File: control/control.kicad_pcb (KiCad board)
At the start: 2 copper layers, 140 x 103.2 mm, 136 parts, among them IC1 TJA1040, IC2 MAX481, IC3 ST232BD, IC4 ATMEGA128-A, IC5 ST232BD, IC6 FT232RL, J4 POWER, P1 SENSOR, P10 DB9, P11 USB_B, P12 USB_M6, P13 DB9, P2 I2C0, P3 I2C1, P4 I2C2, P5 COIN, P6 BILL, P7 ISP, P8 12V, P9 5V, X1 16MHz

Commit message: Updated control board for KiCad 4.0
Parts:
- added R71: DNP, Resistors_SMD:R_0805_HandSoldering, F.Cu at (111.7, 153.8)
- C1, C10, C11, C12, C13, C14, C15, C16, C17, C18, C19, C2, C20, C21, C22, C23, C25, C27, C28, C29, C3, C30, C31, C4, C5, C6, C7, C8, C9: footprint R0805 -> Capacitors_SMD:C_0805_HandSoldering
- C24, C26, C32: footprint C1V5 -> Capacitors_ThroughHole:C_Radial_D5_L11_P2.5
- D1: value RED -> LED805; footprint LED-0805 -> LEDs:LED-0805
- D2, D3: value GREEN -> LED805; footprint LED-0805 -> LEDs:LED-0805
- D4: value TX -> LED805; footprint LED-0805 -> LEDs:LED-0805
- D5: value RX -> LED805; footprint LED-0805 -> LEDs:LED-0805
- IC1: footprint SO8N -> Housings_SOIC:SOIC-8_3.9x4.9mm_Pitch1.27mm
- IC2: value MAX481 -> DNP MAX481CSA; footprint SO8N -> Housings_SOIC:SOIC-8_3.9x4.9mm_Pitch1.27mm
- IC3, IC5: footprint SO16N -> Housings_SOIC:SOIC-16_3.9x9.9mm_Pitch1.27mm
- IC4: footprint TQFP64 -> Housings_QFP:TQFP-64_14x14mm_Pitch0.8mm
- IC6: footprint SSOP28 -> Housings_SSOP:SSOP-28_5.3x10.2mm_Pitch0.65mm
- J4, P1: footprint he10-16ds -> Pin_Headers:Pin_Header_Straight_2x08
- JP1: value FLASH -> 1-2 FLASH EN; footprint SIL-3 -> Pin_Headers:Pin_Header_Straight_1x03
- JP2: value RESET -> 1-2 RESET; footprint SIL-3 -> Pin_Headers:Pin_Header_Straight_1x03
- L1: footprint wuerth_elektronik_v5-WE-PD2_S -> matemat:wuerth_elektronik_v5-WE-PD2_S
- P10, P13: footprint DB9MCS -> matemat:DB9MCS
- P11: footprint USB_B -> Connect:USB_B
- P12: value USB_M6 -> USB_OTG; footprint USB_MINI_B_6 -> Connect:USB_Micro-B
- P2, P3, P4, P5: footprint he10-10ds -> Pin_Headers:Pin_Header_Straight_2x05
- P6: footprint HE10_26DS -> Pin_Headers:Pin_Header_Straight_2x13
- P7: footprint pin_array_3x2 -> Pin_Headers:Pin_Header_Straight_2x03
- P8, P9: footprint Bornier_B2_Phoenix -> matemat:Bornier_B2_Phoenix
- R1, R10, R11, R12, R13, R14, R15, R16, R17, R18, R19, R2, R20, R21, R22, R23, R24, R25, R26, R27, R28, R29, R3, R30, R31, R32, R33, R34, R35, R36, R37, R38, R39, R4, R40, R41, R42, R43, R44, R45, R46, R47, R48, R49, R5, R50, R51, R52, R53, R54, R55, R56, R57, R58, R59, R6, R60, R61, R62, R63, R64, R65, R66, R67, R68, R69, R7, R70, R8, R9: footprint R0805 -> Resistors_SMD:R_0805_HandSoldering
- TP1, TP2, TP3, TP4: footprint TROU3 -> Mounting_Holes:MountingHole_3mm
- X1: footprint Q_49U3HMS -> Crystals:Q_49U3HMS
- moved P6 15.4 mm to (102.1, 62.9), turned to 90 degrees
- moved J4 9.01 mm to (141.1, 126.4), turned to 270 degrees
- moved P1 8.99 mm to (54.7, 86.4), turned to 0 degrees
- moved P2 5.28 mm to (164.3, 121.7), turned to 90 degrees
- moved P3 5.28 mm to (164.3, 138.2), turned to 90 degrees
- moved P4 5.27 mm to (164.3, 154.7), turned to 90 degrees
- moved P5 5.26 mm to (74.5, 62.8), turned to 90 degrees
- moved P11 4.95 mm to (105.6, 144.8), turned to 270 degrees
- moved P7 2.96 mm to (130.4, 111.4), turned to 0 degrees
- moved JP1 2.66 mm to (148.3, 111.2), turned to 0 degrees
- moved JP2 2.60 mm to (143.9, 111.2), turned to 0 degrees
- moved C24 1.41 mm to (110.2, 129.2)
- moved C26 1.30 mm to (121.1, 145.8)
- moved C32 1.20 mm to (126.6, 145.9)
- moved C1 0.42 mm to (161.2, 92.0)
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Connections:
- D1 pad 1: N-0000022 -> GND
- D1 pad 2: GND -> Net-(D1-Pad2)
- D2 pad 1: N-0000030 -> GND
- D2 pad 2: GND -> Net-(D2-Pad2)
- D3 pad 1: N-0000044 -> GND
- D3 pad 2: GND -> Net-(D3-Pad2)
- D4 pad 1: N-0000064 -> GND
- D4 pad 2: GND -> Net-(D4-Pad2)
- D5 pad 1: N-0000061 -> GND
- D5 pad 2: GND -> Net-(D5-Pad2)
- IC6 pad 15: N-0000062 -> Net-(IC6-Pad15)
- IC6 pad 16: N-0000065 -> Net-(IC6-Pad16)
- P11 pad 2: N-0000065 -> Net-(IC6-Pad16)
- P11 pad 3: N-0000062 -> Net-(IC6-Pad15)
- P11 pad 5: (no net) -> Net-(P11-Pad5)
- P12 pad 2: N-0000062 -> Net-(IC6-Pad16)
- P12 pad 3: N-0000065 -> Net-(IC6-Pad15)
- P12 pad 6: GND -> Net-(P11-Pad5)
- R64 pad 2: N-0000022 -> Net-(D1-Pad2)
- R65 pad 2: N-0000030 -> Net-(D2-Pad2)
- R66 pad 2: N-0000044 -> Net-(D3-Pad2)
- R69 pad 2: N-0000064 -> Net-(D4-Pad2)
- R70 pad 2: N-0000061 -> Net-(D5-Pad2)
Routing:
- net Net-(P11-Pad5): track 0.00 -> 29.5 mm
- net Net-(IC6-Pad16): track 0.00 -> 25.7 mm, vias 0 -> 1
- net Net-(IC6-Pad15): track 0.00 -> 25.6 mm, vias 0 -> 2
- net N-0000065: track 23.5 -> 0.00 mm, vias 1 -> 0
- net N-0000062: track 23.4 -> 0.00 mm, vias 1 -> 0
- net Net-(D2-Pad2): track 0.00 -> 5.86 mm
- net GND: track 1197.3 -> 1192.9 mm
- net N-0000030: track 3.20 -> 0.00 mm
- net Net-(D3-Pad2): track 0.00 -> 3.18 mm
- net Net-(D1-Pad2): track 0.00 -> 3.18 mm
- net N-0000044: track 3.18 -> 0.00 mm
- net N-0000022: track 3.18 -> 0.00 mm
- net Net-(IC5-Pad7): track 19.8 -> 22.4 mm
- net Net-(P12-Pad4): track 3.50 -> 5.86 mm
- net Net-(D5-Pad2): track 0.00 -> 2.30 mm
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
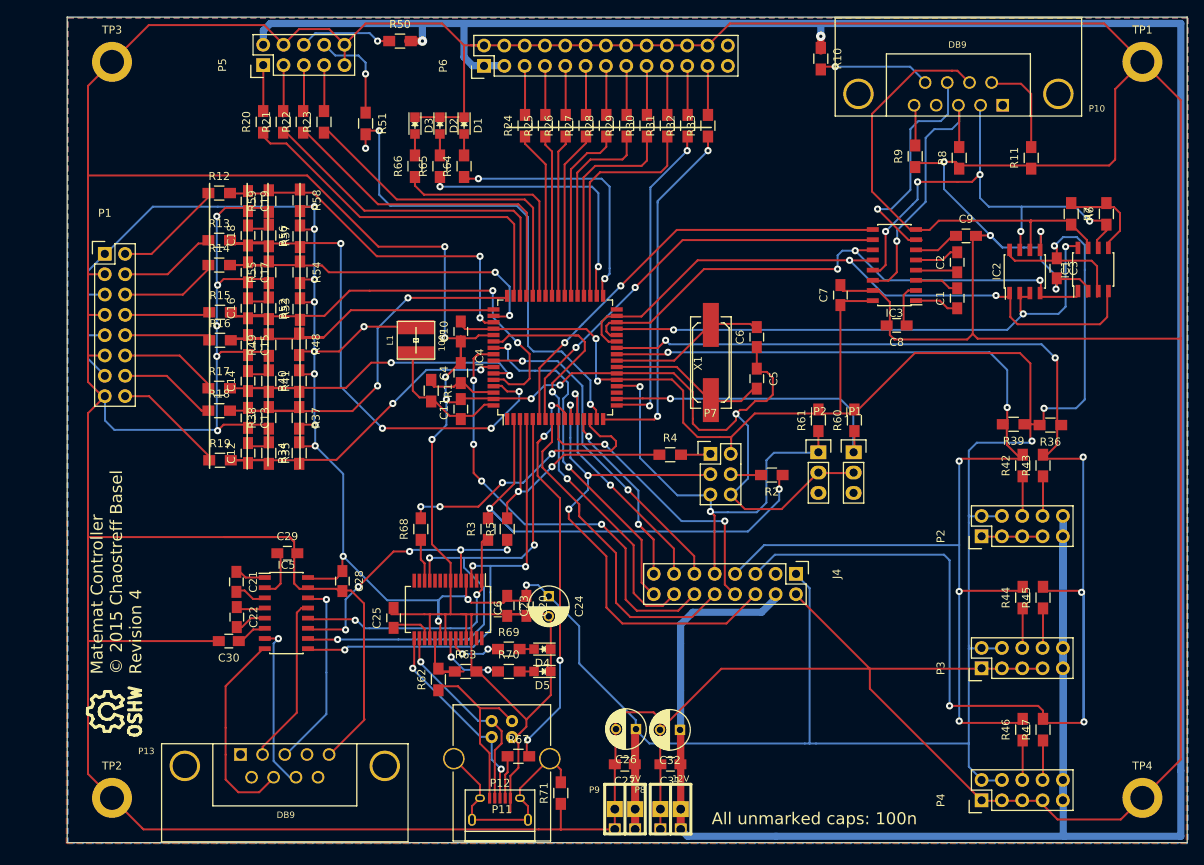
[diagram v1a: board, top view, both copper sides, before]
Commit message: Removed pulldown resistors from analog/digital I/O block to save some space. Removed leftover reference from conversion to KiCad 4.
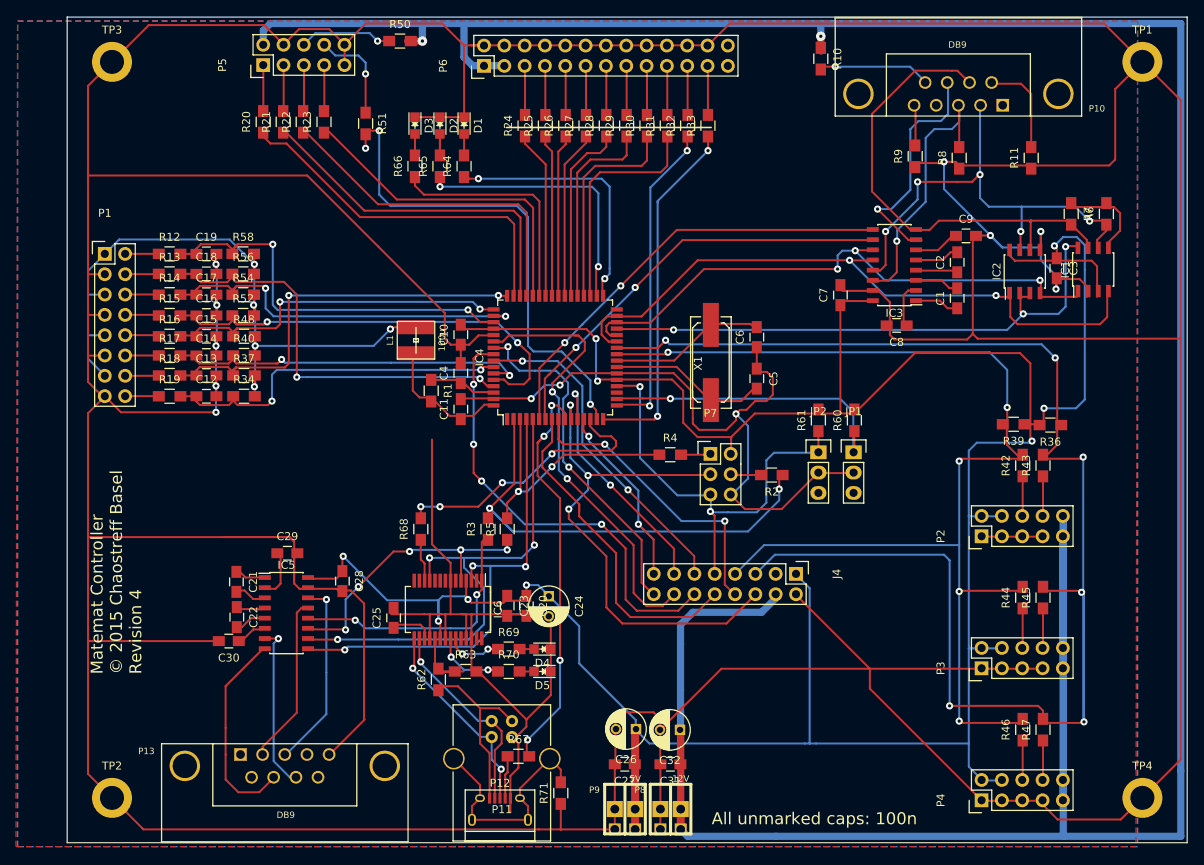
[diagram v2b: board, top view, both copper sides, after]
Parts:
- removed R35, R38, R41, R49, R53, R55, R57, R59: 1k, Resistors_SMD:R_0805_HandSoldering
- removed SYM: Symbol_OSHW-Logo_SilkScreen_07Jul2012, Symbol_OSHW-Logo_SilkScreen_07Jul2012
- moved R19 10.2 mm to (62.8, 104.2)
- moved R34 9.90 mm to (72.1, 104.2), turned to 0 degrees
- moved R12 9.81 mm to (62.8, 86.4)
- moved R58 9.76 mm to (72.0, 86.4), turned to 0 degrees
- moved C12 8.80 mm to (67.4, 104.2), turned to 0 degrees
- moved R37 8.70 mm to (72.1, 101.6), turned to 0 degrees
- moved R56 8.51 mm to (72.0, 88.9), turned to 0 degrees
- moved C19 8.40 mm to (67.4, 86.4), turned to 0 degrees
- moved R54 7.63 mm to (72.0, 91.5), turned to 0 degrees
- moved R40 7.61 mm to (72.1, 99.1), turned to 0 degrees
- moved R18 7.60 mm to (62.8, 101.6)
- moved R13 7.49 mm to (62.8, 88.9)
- moved R17 7.43 mm to (62.8, 99.1)
- moved C13 7.42 mm to (67.4, 101.6), turned to 0 degrees
- moved R14 7.22 mm to (62.8, 91.5)
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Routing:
- net GND: track 1192.9 -> 1122.0 mm, vias 17 -> 12
- net VCC: track 515.9 -> 481.1 mm, vias 18 -> 14
- net /analog_0: track 68.5 -> 53.2 mm, vias 4 -> 2
- net Net-(P1-Pad16): track 14.3 -> 4.25 mm
- net Net-(P1-Pad2): track 14.0 -> 4.21 mm
- net Net-(P1-Pad14): track 12.7 -> 4.28 mm
- net Net-(P1-Pad12): track 12.6 -> 4.21 mm
- net Net-(P1-Pad6): track 12.4 -> 4.23 mm
- net Net-(P1-Pad4): track 12.4 -> 4.28 mm
- net /digital_0: track 44.6 -> 51.1 mm
- net Net-(P1-Pad8): track 11.0 -> 4.48 mm
- net Net-(P1-Pad10): track 11.2 -> 4.88 mm
- net /analog_1: track 58.2 -> 62.5 mm
- net /digital_2: track 43.1 -> 45.5 mm, vias 0 -> 2
- net /digital_3: track 51.9 -> 53.4 mm
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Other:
- net class Default: clearance 0.2 -> 0.15
- net class Power: clearance 0.3 -> 0.25
- rule trace_clearance: 0.2 -> 0.15

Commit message: Updated layout with new/changed parts
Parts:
- added ?: Symbol_OSHW-Logo_SilkScreen, Symbols:Symbol_OSHW-Logo_SilkScreen, F.Cu at (55.1, 143.2)
- added C33: 100n, Capacitors_SMD:C_0805_HandSoldering, F.Cu at (120.4, 86.2)
- added R35: 1k, Resistors_SMD:R_0805_HandSoldering, F.Cu at (135.9, 69.1)
- added R38: 1k, Resistors_SMD:R_0805_HandSoldering, F.Cu at (136.2, 71.7)
- added R41: 1k, Resistors_SMD:R_0805_HandSoldering, F.Cu at (136.4, 74.0)
- added R49: 1k, Resistors_SMD:R_0805_HandSoldering, F.Cu at (136.2, 76.5)
- added R53: 10k, Resistors_SMD:R_0805_HandSoldering, F.Cu at (136.3, 78.5)
- added R55: 10k, Resistors_SMD:R_0805_HandSoldering, F.Cu at (136.2, 81.2)
- added U1: DNP LM2940-N 5V, matemat:SOT-223, F.Cu at (122.1, 137.8)
- JP2: value 1-2 RESET -> RESET; footprint Pin_Headers:Pin_Header_Straight_1x03 -> Pin_Headers:Pin_Header_Straight_1x02
- P5: footprint Pin_Headers:Pin_Header_Straight_2x05 -> Pin_Headers:Pin_Header_Straight_1x17
- P6: value BILL -> CONN_02X13
- R2, R4: value DNP -> 0
- R20, R31: value 100 -> DNP
- R21, R51: value 100 -> 10k
- R22, R23, R24, R25, R26, R27, R32, R33: value 100 -> 1k
- R30: value 100 -> 0
- R61: value 1k -> 10k
- moved P4 17.8 mm to (164.3, 136.9)
- moved R47 14.0 mm to (173.3, 131.9), turned to 0 degrees
- moved R46 14.0 mm to (168.1, 131.9), turned to 180 degrees
- moved P3 8.75 mm to (164.3, 129.4)
- moved R39 7.52 mm to (165.3, 114.6), turned to 0 degrees
- moved R36 6.71 mm to (173.2, 114.5)
- moved R44 5.20 mm to (168.1, 124.3), turned to 180 degrees
- moved R45 5.20 mm to (173.3, 124.3), turned to 0 degrees
- moved R42 4.09 mm to (168.1, 116.7), turned to 180 degrees
- moved R43 4.05 mm to (173.2, 116.7), turned to 0 degrees
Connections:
- net //RST renamed /~RST~
- net /FLASH_EN renamed /~FLASH_EN~
- net /analog_0 renamed /ANALOG_0
- net /analog_1 renamed /ANALOG_1
- net /analog_2 renamed /ANALOG_2
- net /analog_3 renamed /ANALOG_3
- net /digital_0 renamed /DIGITAL_0
- net /digital_1 renamed /DIGITAL_1
- net /digital_2 renamed /DIGITAL_2
- net /digital_3 renamed /DIGITAL_3
- IC4 pad 10: /USBID -> /COIN_INH
- IC4 pad 14: /USB_SLEEP -> /COIN_OUT_F
- IC4 pad 15: /coin_e -> /COIN_OUT_E
- IC4 pad 16: /bill_full -> /BILL_OUT_FULL
- IC4 pad 17: /bill_valid -> /BILL_OUT_VALID
- IC4 pad 30: /UART1_TX -> (no net)
- IC4 pad 31: /UART1_RX -> (no net)
- IC4 pad 32: (no net) -> /USB_SLEEP
- IC4 pad 35: /bill_rej -> /BILL_IN_REJ
- IC4 pad 36: /bill_ack -> /BILL_IN_ACK
- IC4 pad 37: /bill_inh -> /BILL_IN_INH
- IC4 pad 38: /bill_abn -> /BILL_OUT_ABN
- IC4 pad 39: /bill_busy -> /BILL_OUT_BUSY
- IC4 pad 40: /bill_vend3 -> /BILL_OUT_VEND3
- IC4 pad 41: /bill_vend2 -> /BILL_OUT_VEND2
- IC4 pad 42: /bill_vend1 -> /BILL_OUT_VEND1
- IC4 pad 44: /coin_d -> /COIN_OUT_D
- IC4 pad 45: /coin_c -> /COIN_OUT_C
- IC4 pad 46: /coin_b -> /COIN_OUT_B
- IC4 pad 47: /coin_a -> /COIN_OUT_A
- J4 pad 5: /SDA -> Net-(J4-Pad5)
- J4 pad 7: /SCL -> Net-(J4-Pad7)
- P5 pad 1: Net-(P5-Pad1) -> /COIN_OUT_A
- P5 pad 10: GND -> /COIN_INH
- P5 pad 2: +12V -> /COIN_OUT_B
- P5 pad 3: Net-(P5-Pad3) -> GND
- P5 pad 4: GND -> /COIN_OUT_F
- P5 pad 5: Net-(P5-Pad5) -> (no net)
- P5 pad 6: Net-(P5-Pad6) -> /COIN_OUT_E
- P5 pad 7: Net-(P5-Pad7) -> /COIN_OUT_D
- P5 pad 8: Net-(P5-Pad8) -> /COIN_OUT_MODE
- P5 pad 9: GND -> /COIN_OUT_C
- P6 pad 11: Net-(P6-Pad11) -> /BILL_OUT_BUSY
- P6 pad 13: Net-(P6-Pad13) -> /BILL_OUT_ABN
- P6 pad 15: Net-(P6-Pad15) -> VCC
- P6 pad 16: GND -> /BILL_IN_INH
- P6 pad 17: Net-(P6-Pad17) -> VCC
- P6 pad 18: GND -> /BILL_IN_ACK
- P6 pad 19: Net-(P6-Pad19) -> VCC
- P6 pad 20: GND -> /BILL_IN_REJ
- P6 pad 21: Net-(P6-Pad21) -> /BILL_OUT_VALID
- P6 pad 23: Net-(P6-Pad23) -> /BILL_OUT_FULL
- P6 pad 26: (no net) -> GND
- P6 pad 5: Net-(P6-Pad5) -> /BILL_OUT_VEND1
- P6 pad 7: Net-(P6-Pad7) -> /BILL_OUT_VEND2
- P6 pad 9: Net-(P6-Pad9) -> /BILL_OUT_VEND3
- R20 pad 1: /coin_a -> /COIN_OUT_MODE
- R20 pad 2: Net-(P5-Pad1) -> VCC
- R21 pad 1: /coin_b -> /COIN_INH
- R21 pad 2: Net-(P5-Pad3) -> VCC
- R22 pad 1: /coin_c -> /COIN_OUT_A
- R22 pad 2: Net-(P5-Pad5) -> VCC
- R23 pad 1: /coin_d -> /COIN_OUT_B
- R23 pad 2: Net-(P5-Pad7) -> VCC
- R24 pad 1: /bill_vend1 -> /COIN_OUT_F
- R24 pad 2: Net-(P6-Pad5) -> VCC
- R25 pad 1: /bill_vend2 -> /COIN_OUT_E
- R25 pad 2: Net-(P6-Pad7) -> VCC
- R26 pad 1: /bill_vend3 -> /COIN_OUT_D
- R26 pad 2: Net-(P6-Pad9) -> VCC
- R27 pad 1: /bill_busy -> /COIN_OUT_C
- R27 pad 2: Net-(P6-Pad11) -> VCC
- R28 pad 1: /bill_abn -> /SDA
- R28 pad 2: Net-(P6-Pad13) -> Net-(J4-Pad5)
- R29 pad 1: /bill_inh -> /SCL
- R29 pad 2: Net-(P6-Pad15) -> Net-(J4-Pad7)
- R30 pad 1: /bill_ack -> GND
- R30 pad 2: Net-(P6-Pad17) -> /COIN_OUT_MODE
- R31 pad 1: /bill_rej -> GND
- R31 pad 2: Net-(P6-Pad19) -> /COIN_INH
- R32 pad 1: /bill_valid -> /BILL_OUT_VEND1
- R32 pad 2: Net-(P6-Pad21) -> VCC
- R33 pad 1: /bill_full -> /BILL_OUT_VEND2
- R33 pad 2: Net-(P6-Pad23) -> VCC
- R34 pad 2: VCC -> Net-(R34-Pad2)
- R37 pad 2: VCC -> Net-(R34-Pad2)
- R40 pad 2: VCC -> Net-(R34-Pad2)
- R48 pad 2: VCC -> Net-(R34-Pad2)
- R50 pad 1: Net-(P5-Pad6) -> /BILL_OUT_FULL
- R50 pad 2: +12V -> VCC
- R51 pad 1: Net-(P5-Pad8) -> /BILL_IN_INH
- R51 pad 2: /coin_e -> VCC
- R52 pad 2: VCC -> Net-(R34-Pad2)
- R54 pad 2: VCC -> Net-(R34-Pad2)
- R56 pad 2: VCC -> Net-(R34-Pad2)
- R58 pad 2: VCC -> Net-(R34-Pad2)
- R67 pad 2: /USBID -> (no net)
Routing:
- net GND: track 1122.0 -> 785.0 mm, vias 12 -> 11
- net /SDA: track 191.9 -> 91.7 mm, vias 6 -> 2
- net /COIN_INH: track 0.00 -> 85.8 mm, vias 0 -> 4
- net +12V: track 451.6 -> 368.3 mm
- net /COIN_OUT_A: track 0.00 -> 63.0 mm
- net /coin_e: track 62.6 -> 0.00 mm, vias 3 -> 0
- net /SCL: track 148.0 -> 86.1 mm, vias 5 -> 2
- net /BILL_OUT_FULL: track 0.00 -> 61.6 mm, vias 0 -> 3
- net /USBID: track 51.6 -> 0.00 mm, vias 4 -> 0
- net /coin_a: track 45.7 -> 0.00 mm
- net /bill_full: track 45.2 -> 0.00 mm, vias 2 -> 0
- net /coin_b: track 43.9 -> 0.00 mm
- net /coin_c: track 42.6 -> 0.00 mm
- net /coin_d: track 41.1 -> 0.00 mm
- net /bill_valid: track 40.2 -> 0.00 mm, vias 2 -> 0
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- added copper zone on B.Cu, net GND
- added copper zone on F.Cu, net VCC
- removed copper zone on F.Cu, net GND
- removed copper zone on B.Cu, net VCC
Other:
- net class Power: clearance 0.25 -> 0.15
